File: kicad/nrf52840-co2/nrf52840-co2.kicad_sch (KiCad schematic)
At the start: 7 parts

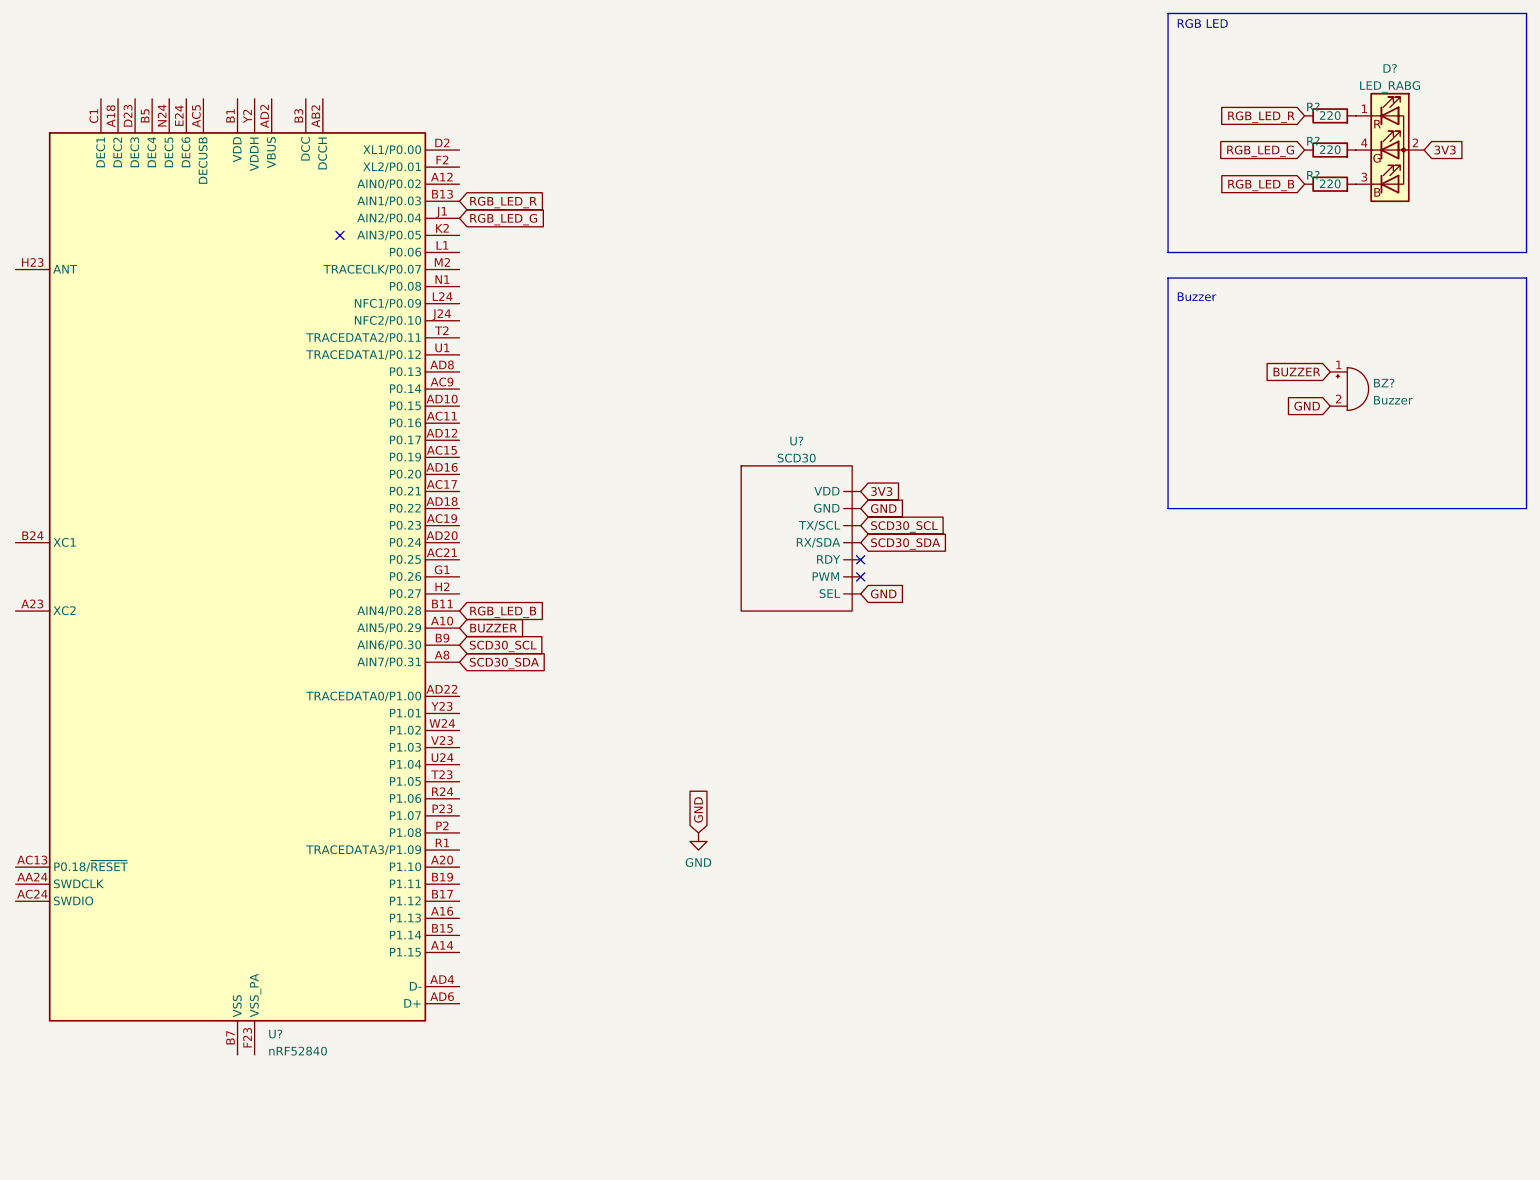
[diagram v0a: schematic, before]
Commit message: Add kicad symbols
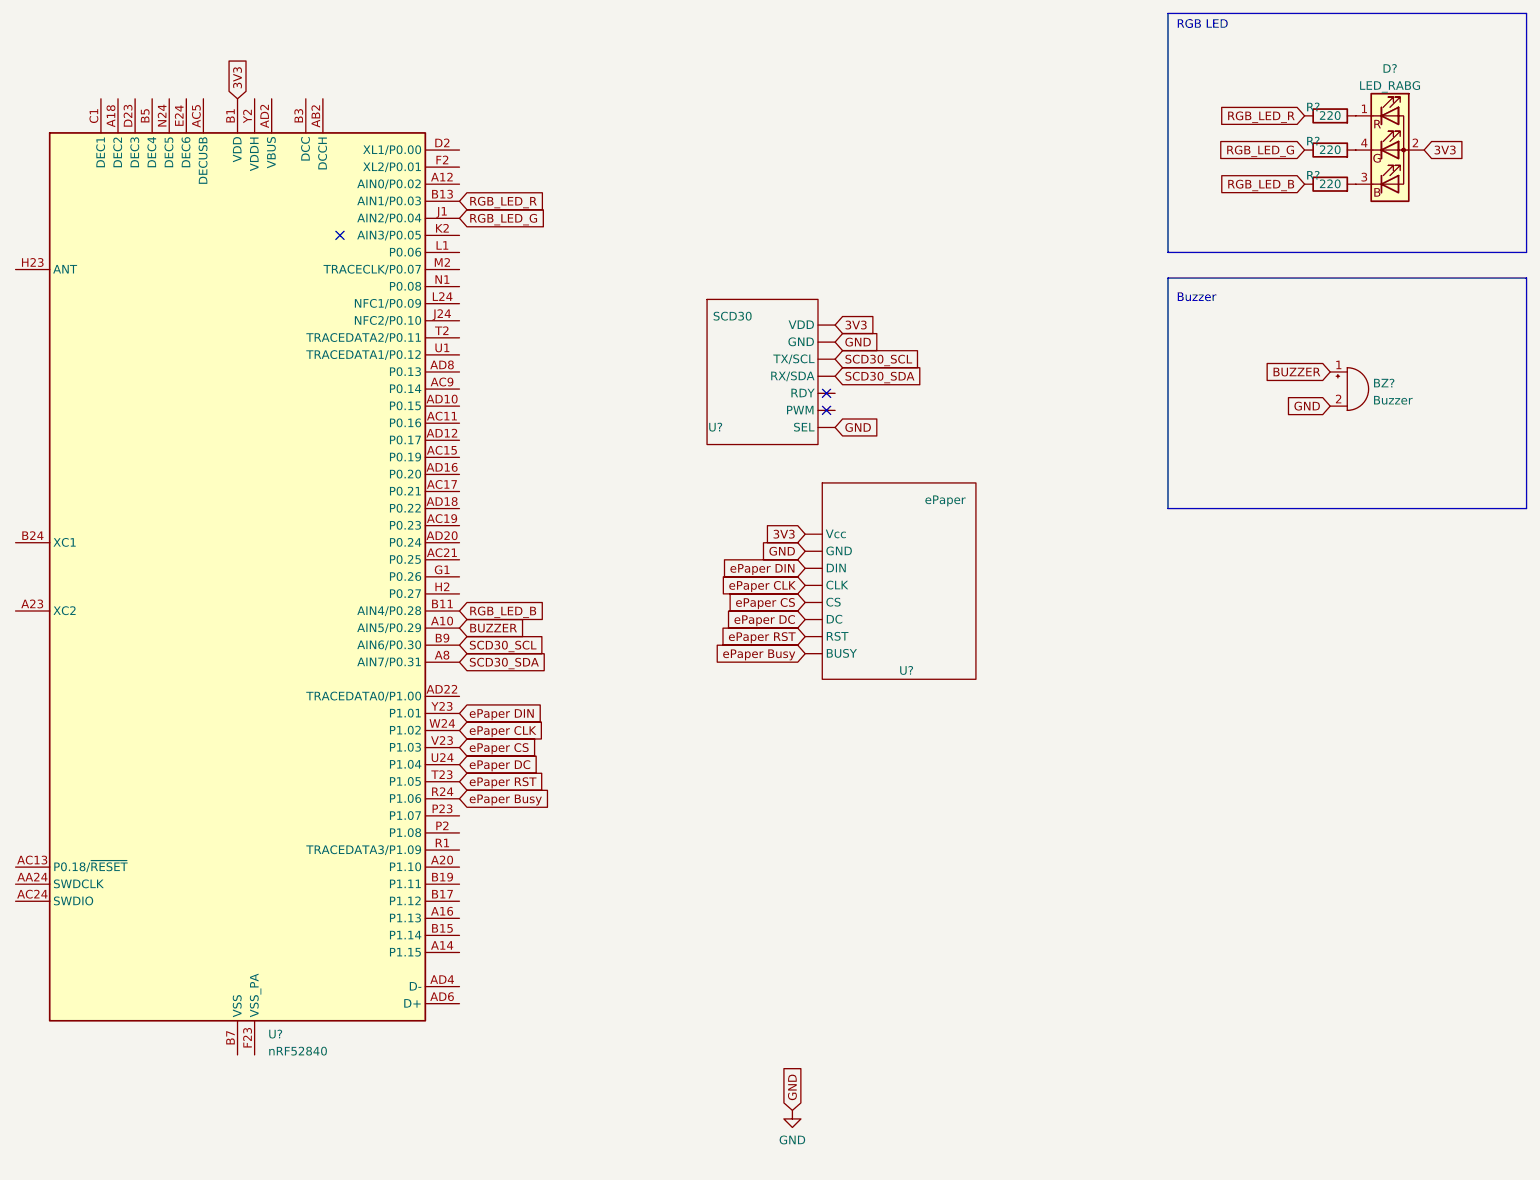
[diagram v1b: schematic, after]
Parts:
- added U?: ePaper, symbol waveshare:ePaper
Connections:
- net 3V3: now also U?.A22 (VDD), U?.AD14 (VDD), U?.AD23 (VDD), U?.B1 (VDD), U?.W1 (VDD), U?. (Vcc)
- net GND: now also U?. (Vcc)
- net ePaper Busy: now reaches U?.R24 (P1.06)
- net ePaper Busy: now also U?. (Vcc)
- net ePaper RST: now reaches U?.T23 (P1.05)
- net ePaper RST: now also U?. (Vcc)
- net ePaper DC: now reaches U?.U24 (P1.04)
- net ePaper DC: now also U?. (Vcc)
- net ePaper CS: now reaches U?.V23 (P1.03)
- net ePaper CS: now also U?. (Vcc)
- net ePaper CLK: now reaches U?.W24 (P1.02)
- net ePaper CLK: now also U?. (Vcc)
- net ePaper DIN: now reaches U?.Y23 (P1.01)
- net ePaper DIN: now also U?. (Vcc)
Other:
- moved on the sheet: U?

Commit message: WIP on the RTIC sample with Interrupt
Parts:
- added U?: KY-040, symbol misc:KY-040
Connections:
- net GND: now also U?. (VCC)
- net Rotary_CLK: now reaches U?.A14 (P1.15)
- net Rotary_CLK: now also U?. (VCC)
- net Rotary_SW: now reaches U?.A16 (P1.13)
- net Rotary_SW: now also U?. (VCC)
- net Rotary_DT: now reaches U?.B15 (P1.14)
- net Rotary_DT: now also U?. (VCC)
- net P0.27: now reaches U?.H2 (P0.27)
- net P0.27: now also U?. (VDD)
- net 3V3 renamed +3V0
- net +3V0: now also U?. (VCC)
- no-connect marks 3 -> 2
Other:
- moved on the sheet: U?
